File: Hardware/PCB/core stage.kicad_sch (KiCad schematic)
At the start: 24 parts, among them IC8 ATXMEGA32A4U, X6 OSCILLATOR

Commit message: MPN & OEPSPN adicionados; ainda em falta novos PNs a ser emitidos
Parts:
- C13: OEPS OEPS010011 -> (none); OEPSPN (none) -> OEPS010011
- C15, R4, R7, R9: OEPS DNI -> (none); OEPSPN (none) -> n.a.
- C16, C25, C26, C27, C28, C29: MPN C1005X7R1H104K050BB -> CGA2B3X7R1H104K050BB; OEPS OEPS010004 -> (none); OEPSPN (none) -> OEPS010016
- IC8: MPN ATXMEGA32A4U-AUR -> ATXMEGA32A4U-A; OEPS OEPS080012 -> (none); OEPSPN (none) -> OEPS080012
- L2, L3: OEPS OEPS040003 -> (none); OEPSPN (none) -> OEPS040003
- R1: OEPS OEPS020037 -> (none); OEPSPN (none) -> OEPS020037
- R34: MPN CRCW040210K0FKED -> ERJ-2RKF1002X; OEPS OEPS020030 -> (none); OEPSPN (none) -> OEPS020013
- STATE0: OEPS OEPS030005 -> (none); OEPSPN (none) -> OEPS030005
- SV2: MPN 609-3210-ND -> PR20203VBDN; OEPS OEPS070015 -> (none); OEPSPN (none) -> OEPS070124
- TP4, TP5, TP6, TP8, TP9: now left out of the parts list
- X6: OEPS OEPS080018 -> (none); OEPSPN (none) -> OEPS080018

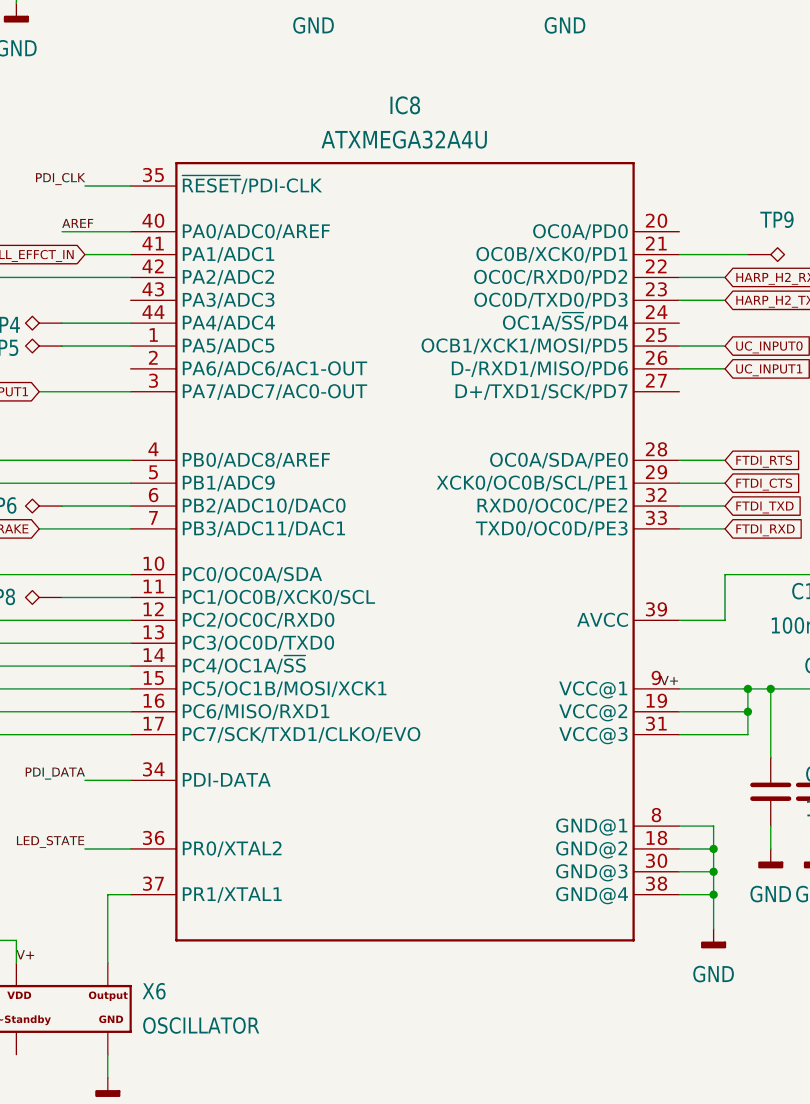
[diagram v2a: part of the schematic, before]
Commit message: MPN & OEPSPN concluded
concluded but not yet certified
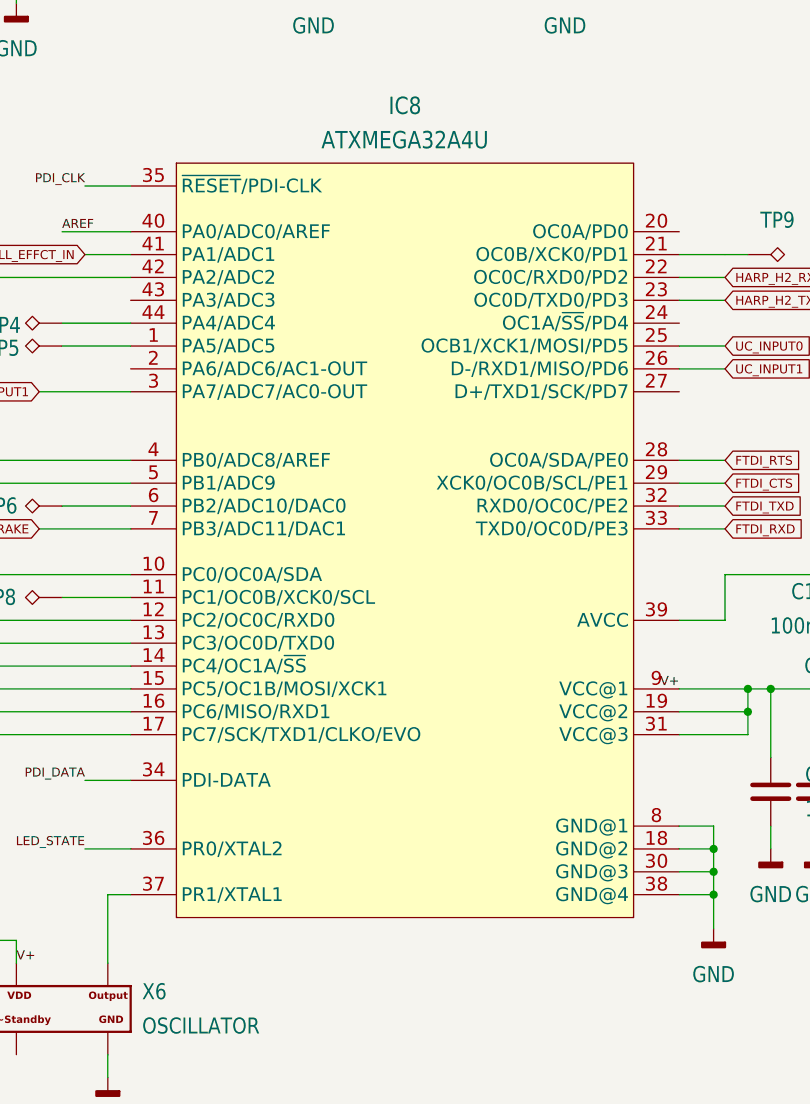
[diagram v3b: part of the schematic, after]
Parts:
- C15, R4, R7, R9: MPN DNI -> n.a.
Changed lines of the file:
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@@
 			)
 		)
-		(property "MPN" "DNI"
+		(property "MPN" "n.a."
 			(at 92.71 34.29 0)
 			(effects
@@
 			)
 		)
-		(property "MPN" "DNI"
+		(property "MPN" "n.a."
 			(at 102.87 48.26 0)
 			(effects
@@
 			)
 		)
-		(property "MPN" "DNI"
+		(property "MPN" "n.a."
 			(at 85.09 25.4 0)
 			(effects
@@
 			)
 		)
-		(property "MPN" "DNI"
+		(property "MPN" "n.a."
 			(at 102.87 33.02 0)
 			(effects
